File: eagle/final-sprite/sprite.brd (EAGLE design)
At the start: 35 x 44.6 mm, 44 parts, among them P1 SPRITE_PIN, P2 SPRITE_PIN, U1 CC430F5137, U2 DRV8833CRTER, X1 TCXO_7Z

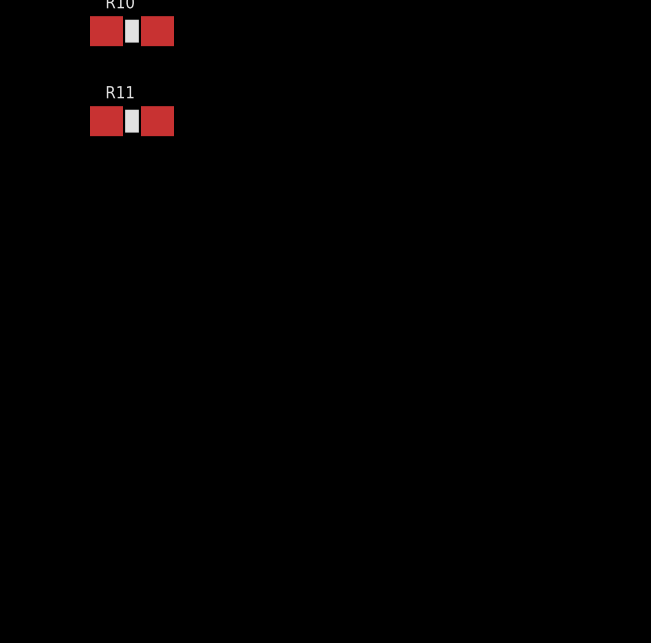
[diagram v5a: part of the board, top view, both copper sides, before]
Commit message: Add second driver
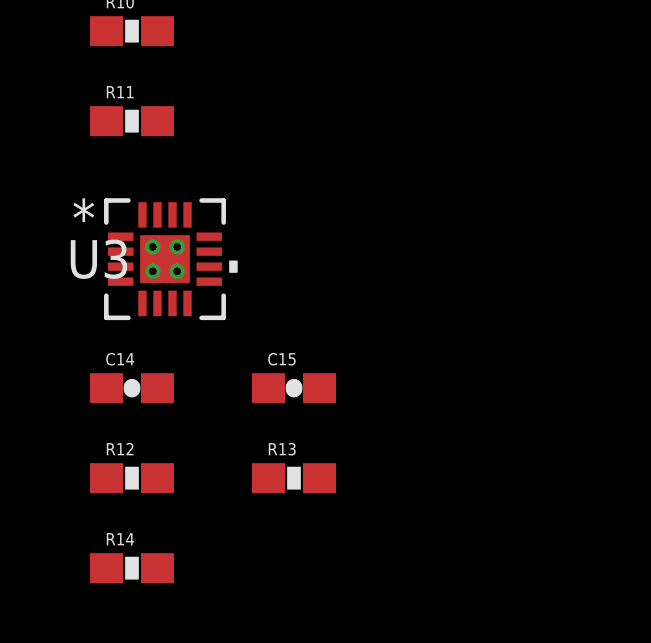
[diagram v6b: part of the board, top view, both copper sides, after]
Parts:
- added C14: 10uF, SparkFun:0603-CAP
- added C15: 2.2uF, SparkFun:0603-CAP
- added R12, R13: 15R, SparkFun:0603-RES
- added R14: 1K, SparkFun:0603-RES
- added U3: DRV8833CRTER, STAC:RTE16_1P66X1P66
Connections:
- new net N$13: C15.1, U3.12
- new net N$14: R12.2, U3.4
- new net N$15: R13.2, U3.1
- net COIL3_EN: now also U3.15
- net COIL3_FAULT_B: now also R14.1, U3.6
- net COIL3_IN1: now also U3.14
- net COIL3_IN2: now also U3.13
- net GND: now also C14.2, C15.2, R12.1, R13.1, U3.11, U3.17
- net VCC: now also R14.2
- net VCCIO: now also C14.1, U3.10
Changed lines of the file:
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@@
 <element name="R10" library="SparkFun" package="0603-RES" value="15R" x="-4.8" y="-110.6"/>
 <element name="R11" library="SparkFun" package="0603-RES" value="1K" x="-4.8" y="-113.6"/>
+<element name="U3" library="STAC" package="RTE16_1P66X1P66" value="DRV8833CRTER" x="-3.7" y="-118.2">
+<attribute name="AUTHOR" value="Ultra-Librarian" x="-3.7" y="-118.2" size="1.778" layer="27" display="off"/>
+<attribute name="CHECKED" value="Kevin Zheng" x="-3.7" y="-118.2" size="1.778" layer="27" display="off"/>
+<attribute name="DIGI-KEY_PN" value="296-40079-1-ND" x="-3.7" y="-118.2" size="1.778" layer="27" display="off"/>
+<attribute name="MANUFACTURER_PART_NUMBER" value="DRV8833CRTER" x="-3.7" y="-118.2" size="1.778" layer="27" display="off"/>
+<attribute name="VENDOR" value="Texas Instruments" x="-3.7" y="-118.2" size="1.778" layer="27" display="off"/>
+</element>
+<element name="C14" library="SparkFun" package="0603-CAP" value="10uF" x="-4.8" y="-122.5"/>
+<element name="C15" library="SparkFun" package="0603-CAP" value="2.2uF" x="0.6" y="-122.5"/>
+<element name="R12" library="SparkFun" package="0603-RES" value="15R" x="-4.8" y="-125.5"/>
+<element name="R13" library="SparkFun" package="0603-RES" value="15R" x="0.6" y="-125.5"/>
+<element name="R14" library="SparkFun" package="0603-RES" value="1K" x="-4.8" y="-128.5"/>
 </elements>
 <signals>
@@
 <contactref element="U$4" pad="16"/>
 <contactref element="R11" pad="2"/>
+<contactref element="R14" pad="2"/>
+<wire x1="-3.95" y1="-113.6" x2="-3.95" y2="-128.5" width="0" layer="19" extent="1-1"/>
 <wire x1="-0.82" y1="-90.15" x2="-3.95" y2="-113.6" width="0" layer="19" extent="1-1"/>
 <wire x1="0.45" y1="-84.8" x2="-0.82" y2="-90.15" width="0" layer="19" extent="1-1"/>
@@
 <contactref element="R9" pad="1"/>
 <contactref element="R10" pad="1"/>
+<contactref element="U3" pad="11"/>
+<contactref element="U3" pad="17"/>
+<contactref element="C14" pad="2"/>
+<contactref element="C15" pad="2"/>
+<contactref element="R12" pad="1"/>
+<contactref element="R13" pad="1"/>
+<wire x1="-3.95" y1="-122.5" x2="-5.65" y2="-125.5" width="0" layer="19" extent="1-1"/>
+<wire x1="-3.7" y1="-118.2" x2="-3.95" y2="-122.5" width="0" layer="19" extent="1-1"/>
+<wire x1="-2.225" y1="-117.95" x2="-3.7" y2="-118.2" width="0" layer="19" extent="1-1"/>
+<wire x1="-0.25" y1="-125.5" x2="-3.95" y2="-122.5" width="0" layer="19" extent="1-1"/>
+<wire x1="1.45" y1="-122.5" x2="-0.25" y2="-125.5" width="0" layer="19" extent="1-1"/>
+<wire x1="-5.65" y1="-110.6" x2="-3.7" y2="-118.2" width="0" layer="19" extent="1-1"/>
 <wire x1="-5.65" y1="-107.6" x2="-5.65" y2="-110.6" width="0" layer="19" extent="1-1"/>
 <wire x1="-3.95" y1="-104.6" x2="-5.65" y2="-107.6" width="0" layer="19" extent="1-1"/>
@@
 <contactref element="C12" pad="1"/>
 <contactref element="U2" pad="10"/>
+<contactref element="C14" pad="1"/>
+<contactref element="U3" pad="10"/>
+<wire x1="-2.225" y1="-118.45" x2="-5.65" y2="-122.5" width="0" layer="19" extent="1-1"/>
+<wire x1="-5.65" y1="-101.6" x2="-2.225" y2="-118.45" width="0" layer="19" extent="1-1"/>
 <wire x1="-2.225" y1="-97.55" x2="-5.65" y2="-101.6" width="0" layer="19" extent="1-1"/>
 <wire x1="-0.82" y1="-91.15" x2="-2.225" y2="-97.55" width="0" layer="19" extent="1-1"/>
@@
 <signal name="COIL3_IN1">
 <contactref element="U1" pad="2"/>
+<contactref element="U3" pad="14"/>
+<wire x1="9.077815625" y1="22.1402" x2="-3.4499375" y2="-116.725" width="0" layer="19" extent="1-1"/>
 </signal>
 <signal name="COIL3_IN2">
 <contactref element="U1" pad="1"/>
+<contactref element="U3" pad="13"/>
+<wire x1="8.7242625" y1="21.786646875" x2="-2.9498125" y2="-116.725" width="0" layer="19" extent="1-1"/>
 </signal>
 <signal name="N$8">
@@
 <signal name="COIL3_EN">
 <contactref element="U1" pad="48"/>
+<contactref element="U3" pad="15"/>
+<wire x1="7.875734375" y1="21.786646875" x2="-3.9500625" y2="-116.725" width="0" layer="19" extent="1-1"/>
 </signal>
 <signal name="COIL12_FAULT_B">
@@
 <signal name="COIL3_FAULT_B">
 <contactref element="U1" pad="12"/>
+<contactref element="U3" pad="6"/>
+<contactref element="R14" pad="1"/>
+<wire x1="-3.9500625" y1="-119.675" x2="-5.65" y2="-128.5" width="0" layer="19" extent="1-1"/>
+<wire x1="12.61335" y1="25.675734375" x2="-3.9500625" y2="-119.675" width="0" layer="19" extent="1-1"/>
 </signal>
 <signal name="N$9">
@@
 <wire x1="-5.175" y1="-96.55" x2="-3.95" y2="-110.6" width="0" layer="19" extent="1-1"/>
 </signal>
+<signal name="N$13">
+<contactref element="C15" pad="1"/>
+<contactref element="U3" pad="12"/>
+<wire x1="-2.225" y1="-117.45" x2="-0.25" y2="-122.5" width="0" layer="19" extent="1-1"/>
+</signal>
+<signal name="N$14">
+<contactref element="R12" pad="2"/>
+<contactref element="U3" pad="4"/>
+<wire x1="-5.175" y1="-118.95" x2="-3.95" y2="-125.5" width="0" layer="19" extent="1-1"/>
+</signal>
+<signal name="N$15">
+<contactref element="R13" pad="2"/>
+<contactref element="U3" pad="1"/>
+<wire x1="-5.175" y1="-117.45" x2="1.45" y2="-125.5" width="0" layer="19" extent="1-1"/>
+</signal>
 </signals>

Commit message: adding power stuff
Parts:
- added C16, C17: (no value), resistor:C0402
- added R15, R16, R17, R18, R19, R20, R21, R22, R23: (no value), resistor:R0402
- added U$5: LPS4018-223M, STAC:LPS4018-223M
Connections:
- new net DSW: U$4.22, U1.24
- new net N$18: R16.2, R17.1, U$4.9
- new net N$20: R15.2, U$4.21
- new net N$21: C16.1, U$4.8
- new net N$22: U$4.13, U$5.P$2
- new net REF: R18.2, R20.2, U$4.1
- new net REG_D0: U$4.23, U1.3
- new net REG_D1: U$4.24, U1.4
- new net SETHYS: R21.1, R22.2, U$4.6
- new net SETPG: R20.1, R21.2, U$4.5
- new net SETSD: R19.2, R23.1, U$4.2
- new net TERM: R18.1, R23.2, U$4.4
- new net VID: U$4.20, U1.23
- net GND: now also C16.2, C17.2, R15.1, R16.1, R19.1, R22.1, U$4.3
- net PGOOD: now also U1.46
- net REGGOOD: now also U1.47
- net VCCINT: now also C17.1, R17.2, U$4.10, U$5.P$1

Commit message: changed passives to 0402 in schematic
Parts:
- removed C11: 10uF, SparkFun:0805
- removed C12, C14: 10uF, SparkFun:0603-CAP
- removed C13, C15: 2.2uF, SparkFun:0603-CAP
- removed R12, R13: 15R, SparkFun:0603-RES
- removed R14: 1K, SparkFun:0603-RES
- added C18: 10uF, rcl:C0402
- added C19, C20, C22: 0.1uF, rcl:C0402
- added C21: 10nF, rcl:C0402
- added R24, R25: 10K, rcl:R0402
- added R26: 1K, rcl:R0402
- C1: value 10 nF -> 10uF; device SparkFun:0603-CAP -> rcl:C0402
- C10: value 0.1uF -> 2.2uF; device SparkFun:0805 -> rcl:C0402
- C2: value 470nF -> 2.2uF; device SparkFun:0603-CAP -> rcl:C0402
- C3: value 470nF -> 2.2nF; device SparkFun:0603-CAP -> rcl:C0402
- C4: value 2.2nF -> 470nF; device SparkFun:0603-CAP -> rcl:C0402
- C7: value 0.1uF -> 470nF; device SparkFun:0805 -> rcl:C0402
- C8: device SparkFun:0805 -> rcl:C0402
- C9: value 0.1uF -> 10uF; device SparkFun:0805 -> rcl:C0402
- R1: value 56K -> 15R; device SparkFun:0603-RES -> rcl:R0402
- R10, R9: value 15R -> 1K; device SparkFun:0603-RES -> rcl:R0402
- R11: device SparkFun:0603-RES -> rcl:R0402
- R2: value 47K -> 56K; device SparkFun:0603-RES -> rcl:R0402
- R3, R4, R6: device SparkFun:0805 -> rcl:R0402
- R5: value 270R -> 47K; device SparkFun:0603-RES -> rcl:R0402
- R7: value 10K -> 270R; device SparkFun:0805 -> rcl:R0402
- R8: value 10K -> 15R; device SparkFun:0805 -> rcl:R0402
- moved C2 297.0 mm to (-9.00, -270.2), turned to 0 degrees
- moved C1 292.1 mm to (-9.00, -260.4)
- moved R1 292.1 mm to (-9.30, -265.3), turned to 0 degrees
- moved C4 272.3 mm to (-9.00, -250.6), flipped to the top
- moved R5 269.7 mm to (-9.30, -240.8), turned to 0 degrees
- moved R2 267.4 mm to (-9.30, -245.7)
- moved C3 267.4 mm to (-9.00, -235.9), turned to 0 degrees
- moved C10 208.6 mm to (-9.00, -289.8)
- moved C9 203.6 mm to (-9.00, -284.9)
- moved R8 198.7 mm to (-9.30, -275.1)
- moved C8 191.8 mm to (-9.00, -255.5)
- moved R11 186.1 mm to (-9.30, -299.6)
- moved R10 184.2 mm to (-9.30, -294.7)
- moved R9 172.5 mm to (-9.30, -280.0)
- moved C7 162.7 mm to (-9.00, -226.1)
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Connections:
- net COIL12_FAULT_B: now also R9.1; no longer R11.1
- net COIL3_FAULT_B: now also R26.1; no longer R14.1
- net GND: now also C1.2, C18.2, C19.2, C20.2, C21.2, C22.2, C3.1, C4.2, R1.1, R11.1, R2.1, R25.1, R6.1; no longer C11.2, C12.2, C13.2, C14.2, C15.2, C3.2, C4.1, C8.2, R1.2, R12.1, R13.1, R7.1, R9.1
- net N$1: now also C8.1; no longer C1.1
- net N$10: now also R1.2; no longer R10.2
- net N$11: now also R7.1; no longer R5.1
- net N$12: now also C8.2; no longer C1.2
- net N$13: now also C10.1; no longer C15.1
- net N$14: now also R10.2; no longer R12.2
- net N$15: now also R11.2; no longer R13.2
- net N$2: now also R7.2; no longer R5.2
- net N$3: now also R2.2; no longer R1.1
- net N$4: now also C7.1; no longer C3.1
- net N$5: now also C22.1; no longer C7.1
- net N$6: now also C21.1; no longer C8.1
- net N$7: now also R24.1; no longer R3.1
- net N$8: now also C2.1; no longer C13.1
- net N$9: now also R8.2; no longer R9.2
- net P2.0/A0: now also R6.2; no longer R7.2
- net P2.5/A5: now also R25.2; no longer R8.2
- net RST: now also C3.2, R5.1; no longer C4.2, R2.1
- net SCL: now also R4.1; no longer R6.1
- net SDA: now also R3.1; no longer R4.1
- net VCC: now also C18.1, C19.1, C20.1, C4.1, R24.2, R26.2, R5.2, R9.2; no longer C10.1, C11.1, C2.1, C9.1, R11.2, R14.2, R2.2, R6.2
- net VCCIO: now also C1.1, C9.1; no longer C12.1, C14.1
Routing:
- net GND: track 29.9 -> 22.5 mm, vias 6 -> 4
- net N$2: track 3.53 -> 1.16 mm
- net N$4: track 12.1 -> 9.82 mm
- net N$1: track 2.92 -> 0.83 mm
- net N$11: track 1.77 -> 0.07 mm
- net N$12: track 1.37 -> 0.04 mm
- net RST: track 2.89 -> 1.84 mm
- net N$3: track 5.26 -> 4.41 mm
